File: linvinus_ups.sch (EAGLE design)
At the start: 19 parts, among them J1 BATTERY_CONNDEANS, Q1 IRF7240PBF, Q2 IRF7240PBF, Q3 BSS123, Q4 IRF7240PBF, Q5 FDN360P

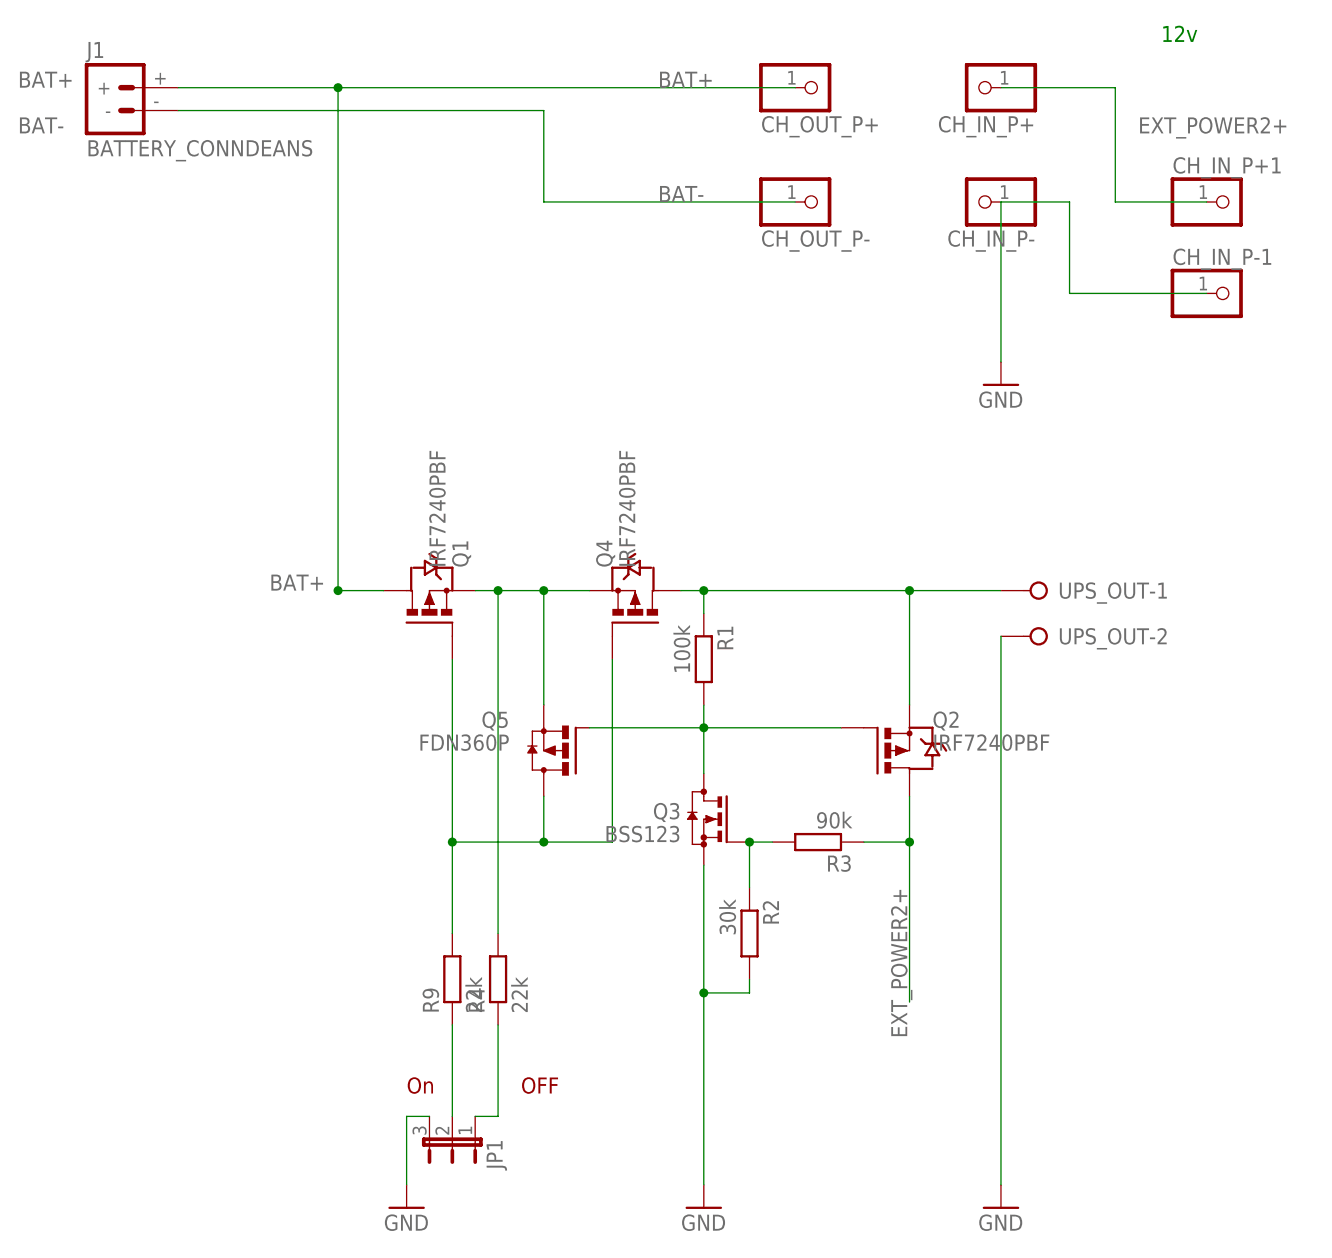
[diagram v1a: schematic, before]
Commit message: fix v2, completely close Q4 if vbatt > external power
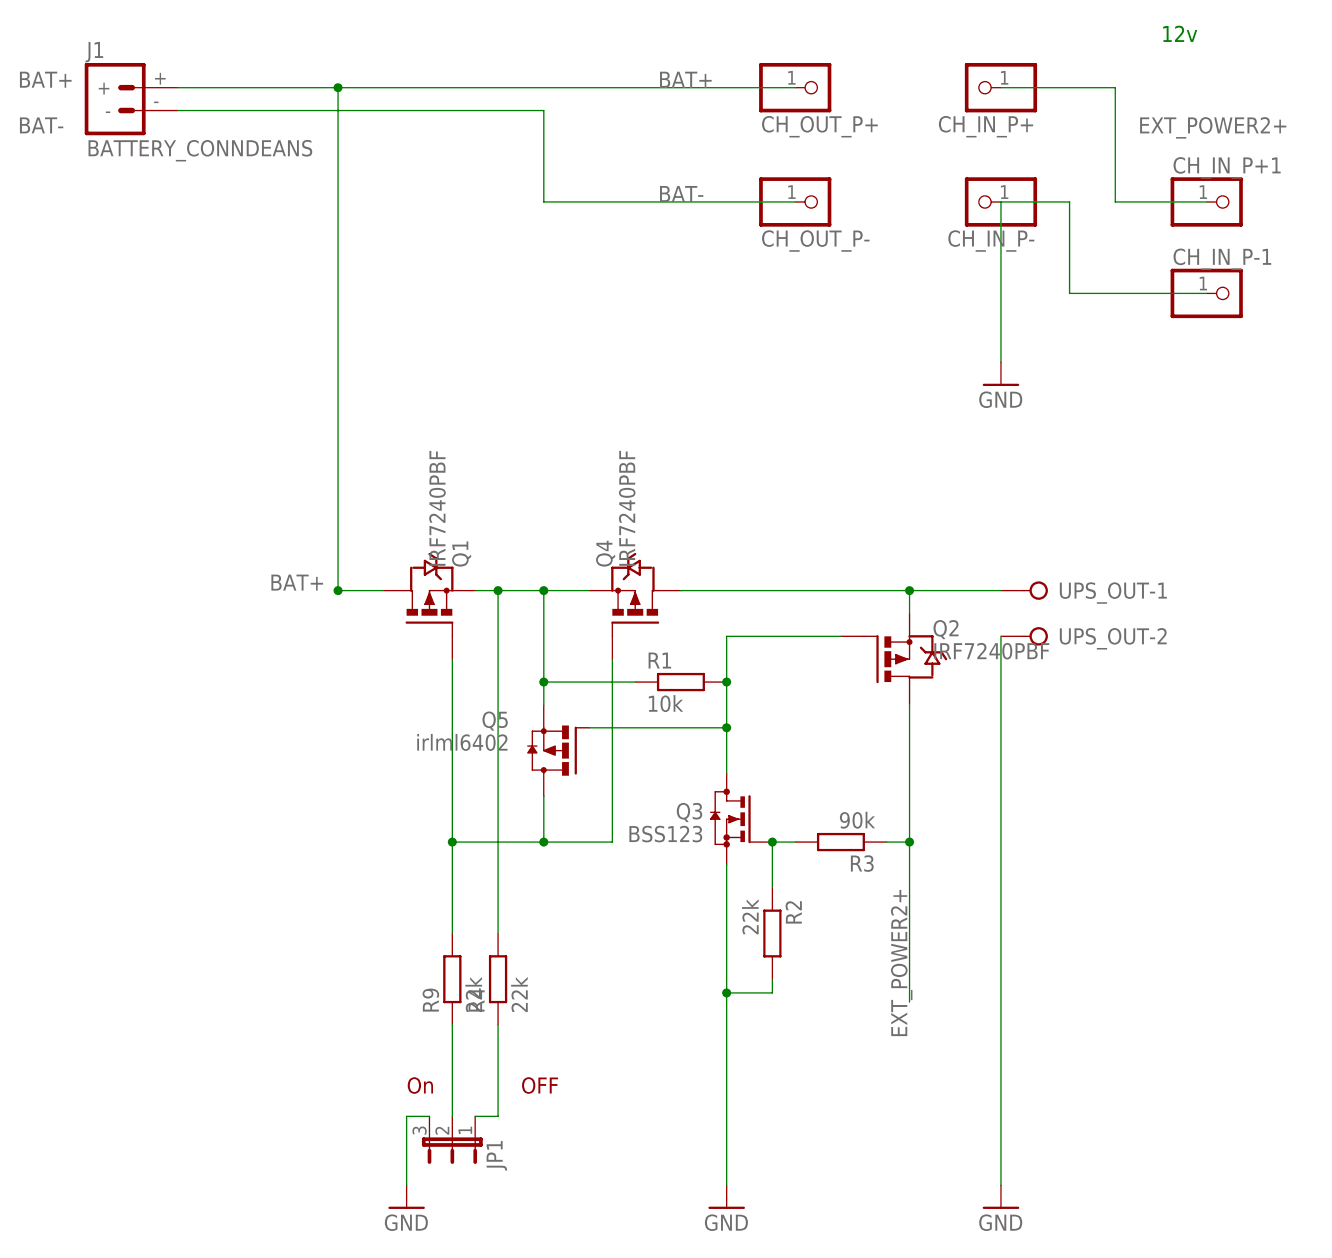
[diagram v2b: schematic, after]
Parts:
- Q5: value FDN360P -> irlml6402
- R1: value 100k -> 10k
- R2: value 30k -> 22k
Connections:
- net N$5: now also R1.1
- net N$6: no longer R1.1
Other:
- moved on the sheet: Q2, Q3, R1, R2, R3
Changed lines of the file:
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@@
 <part name="Q2" library="transistor-power" deviceset="P-MOSFET-SO8" device="" value="IRF7240PBF"/>
 <part name="Q3" library="transistor-small-signal" deviceset="BSS123" device=""/>
-<part name="R1" library="resistor" deviceset="R-EU_" device="R0805" value="100k"/>
-<part name="R2" library="resistor" deviceset="R-EU_" device="R0805" value="30k"/>
+<part name="R1" library="resistor" deviceset="R-EU_" device="R0805" value="10k"/>
+<part name="R2" library="resistor" deviceset="R-EU_" device="R0805" value="22k"/>
 <part name="R3" library="resistor" deviceset="R-EU_" device="R0805" value="90k"/>
 <part name="GND2" library="supply1" deviceset="GND" device=""/>
@@
 <part name="R4" library="resistor" deviceset="R-EU_" device="R0805" value="22k"/>
 <part name="JP1" library="jumper" deviceset="JP2E" device=""/>
-<part name="Q5" library="transistor-power" deviceset="FDN360P" device=""/>
+<part name="Q5" library="transistor-power" deviceset="FDN360P" device="" value="irlml6402"/>
 </parts>
 <sheets>
@@
 <wire x1="132.08" y1="50.8" x2="40.64" y2="50.8" width="0.1524" layer="98"/>
 <wire x1="40.64" y1="50.8" x2="40.64" y2="-35.56" width="0.1524" layer="98"/>
-<text x="93.98" y="-22.86" size="6.4516" layer="98">UPS</text>
+<text x="68.58" y="-30.48" size="6.4516" layer="98">UPS</text>
 </plain>
 <instances>
@@
 <instance part="R9" gate="G$1" x="63.5" y="0" rot="R90"/>
 <instance part="GND7" gate="1" x="124.46" y="-25.4"/>
-<instance part="Q2" gate="G$1" x="111.76" y="25.4"/>
-<instance part="Q3" gate="G$1" x="91.44" y="17.78" rot="MR0"/>
-<instance part="R1" gate="G$1" x="91.44" y="35.56" rot="R270"/>
-<instance part="R2" gate="G$1" x="96.52" y="5.08" rot="R270"/>
-<instance part="R3" gate="G$1" x="104.14" y="15.24" rot="R180"/>
-<instance part="GND2" gate="1" x="91.44" y="-25.4"/>
+<instance part="Q2" gate="G$1" x="111.76" y="35.56"/>
+<instance part="Q3" gate="G$1" x="93.98" y="17.78" rot="MR0"/>
+<instance part="R1" gate="G$1" x="88.9" y="33.02"/>
+<instance part="R2" gate="G$1" x="99.06" y="5.08" rot="R270"/>
+<instance part="R3" gate="G$1" x="106.68" y="15.24" rot="R180"/>
+<instance part="GND2" gate="1" x="93.98" y="-25.4"/>
 <instance part="J1" gate="G$1" x="25.4" y="99.06"/>
 <instance part="CH_IN_P+1" gate="G$1" x="149.86" y="86.36"/>
@@
 <segment>
 <label x="112.268" y="10.16" size="1.778" layer="95" rot="R270"/>
-<wire x1="114.3" y1="20.32" x2="114.3" y2="15.24" width="0.1524" layer="91"/>
+<wire x1="114.3" y1="30.48" x2="114.3" y2="15.24" width="0.1524" layer="91"/>
 <pinref part="Q2" gate="G$1" pin="D"/>
 <pinref part="R3" gate="G$1" pin="1"/>
 <wire x1="114.3" y1="15.24" x2="114.3" y2="-2.54" width="0.1524" layer="91"/>
-<wire x1="109.22" y1="15.24" x2="114.3" y2="15.24" width="0.1524" layer="91"/>
+<wire x1="111.76" y1="15.24" x2="114.3" y2="15.24" width="0.1524" layer="91"/>
 <junction x="114.3" y="15.24"/>
 </segment>
@@
 <pinref part="Q3" gate="G$1" pin="S"/>
 <pinref part="GND2" gate="1" pin="GND"/>
-<wire x1="91.44" y1="12.7" x2="91.44" y2="-1.524" width="0.1524" layer="91"/>
+<wire x1="93.98" y1="12.7" x2="93.98" y2="-1.524" width="0.1524" layer="91"/>
 <pinref part="R2" gate="G$1" pin="2"/>
-<wire x1="91.44" y1="-1.524" x2="91.44" y2="-22.86" width="0.1524" layer="91"/>
-<wire x1="96.52" y1="0" x2="96.52" y2="-1.524" width="0.1524" layer="91"/>
-<wire x1="96.52" y1="-1.524" x2="91.44" y2="-1.524" width="0.1524" layer="91"/>
-<junction x="91.44" y="-1.524"/>
+<wire x1="93.98" y1="-1.524" x2="93.98" y2="-22.86" width="0.1524" layer="91"/>
+<wire x1="99.06" y1="0" x2="99.06" y2="-1.524" width="0.1524" layer="91"/>
+<wire x1="99.06" y1="-1.524" x2="93.98" y2="-1.524" width="0.1524" layer="91"/>
+<junction x="93.98" y="-1.524"/>
 </segment>
 <segment>
@@
 <pinref part="R1" gate="G$1" pin="2"/>
 <pinref part="Q3" gate="G$1" pin="D"/>
-<wire x1="91.44" y1="30.48" x2="91.44" y2="27.94" width="0.1524" layer="91"/>
+<wire x1="93.98" y1="33.02" x2="93.98" y2="27.94" width="0.1524" layer="91"/>
 <pinref part="Q5" gate="G$1" pin="G"/>
-<wire x1="91.44" y1="27.94" x2="91.44" y2="22.86" width="0.1524" layer="91"/>
-<wire x1="78.74" y1="27.94" x2="91.44" y2="27.94" width="0.1524" layer="91"/>
-<junction x="91.44" y="27.94"/>
+<wire x1="93.98" y1="27.94" x2="93.98" y2="22.86" width="0.1524" layer="91"/>
+<wire x1="78.74" y1="27.94" x2="93.98" y2="27.94" width="0.1524" layer="91"/>
+<junction x="93.98" y="27.94"/>
 <pinref part="Q2" gate="G$1" pin="G"/>
-<wire x1="106.68" y1="27.94" x2="91.44" y2="27.94" width="0.1524" layer="91"/>
+<wire x1="106.68" y1="38.1" x2="93.98" y2="38.1" width="0.1524" layer="91"/>
+<wire x1="93.98" y1="38.1" x2="93.98" y2="33.02" width="0.1524" layer="91"/>
+<junction x="93.98" y="33.02"/>
 </segment>
 </net>
@@
 <pinref part="R3" gate="G$1" pin="2"/>
 <pinref part="Q3" gate="G$1" pin="G"/>
-<wire x1="99.06" y1="15.24" x2="96.52" y2="15.24" width="0.1524" layer="91"/>
+<wire x1="101.6" y1="15.24" x2="99.06" y2="15.24" width="0.1524" layer="91"/>
 <pinref part="R2" gate="G$1" pin="1"/>
-<wire x1="96.52" y1="10.16" x2="96.52" y2="15.24" width="0.1524" layer="91"/>
-<junction x="96.52" y="15.24"/>
+<wire x1="99.06" y1="10.16" x2="99.06" y2="15.24" width="0.1524" layer="91"/>
+<junction x="99.06" y="15.24"/>
 </segment>
 </net>
@@
 <junction x="68.58" y="43.18"/>
 <pinref part="Q5" gate="G$1" pin="S"/>
-<wire x1="73.66" y1="30.48" x2="73.66" y2="43.18" width="0.1524" layer="91"/>
+<wire x1="73.66" y1="30.48" x2="73.66" y2="33.02" width="0.1524" layer="91"/>
 <junction x="73.66" y="43.18"/>
+<pinref part="R1" gate="G$1" pin="1"/>
+<wire x1="73.66" y1="33.02" x2="73.66" y2="43.18" width="0.1524" layer="91"/>
+<wire x1="83.82" y1="33.02" x2="73.66" y2="33.02" width="0.1524" layer="91"/>
+<junction x="73.66" y="33.02"/>
 </segment>
 </net>
@@
 <pinref part="Q4" gate="G$1" pin="D"/>
 <pinref part="UPS_OUT" gate="-1" pin="KL"/>
-<wire x1="88.9" y1="43.18" x2="91.44" y2="43.18" width="0.1524" layer="91"/>
-<pinref part="R1" gate="G$1" pin="1"/>
-<wire x1="91.44" y1="43.18" x2="114.3" y2="43.18" width="0.1524" layer="91"/>
+<wire x1="88.9" y1="43.18" x2="114.3" y2="43.18" width="0.1524" layer="91"/>
 <wire x1="114.3" y1="43.18" x2="124.46" y2="43.18" width="0.1524" layer="91"/>
-<wire x1="91.44" y1="40.64" x2="91.44" y2="43.18" width="0.1524" layer="91"/>
 <pinref part="Q2" gate="G$1" pin="S"/>
-<wire x1="114.3" y1="30.48" x2="114.3" y2="43.18" width="0.1524" layer="91"/>
+<wire x1="114.3" y1="40.64" x2="114.3" y2="43.18" width="0.1524" layer="91"/>
 <junction x="114.3" y="43.18"/>
-<junction x="91.44" y="43.18"/>
-</segment>
-</net>
+</segment>
+</net>
